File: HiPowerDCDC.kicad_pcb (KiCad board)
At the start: 2 copper layers, 125.8 x 100 mm, 66 parts, among them J1 Conn_01x01, J2 Conn_01x01, J3 Conn_01x01, J4 Conn_01x01, J5 Conn_01x04, Q1 WMJ38N60, Q2 WMJ38N60, SW1 SW_Push, SW2 SW_Push, U1 ESP32-WROOM-32U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

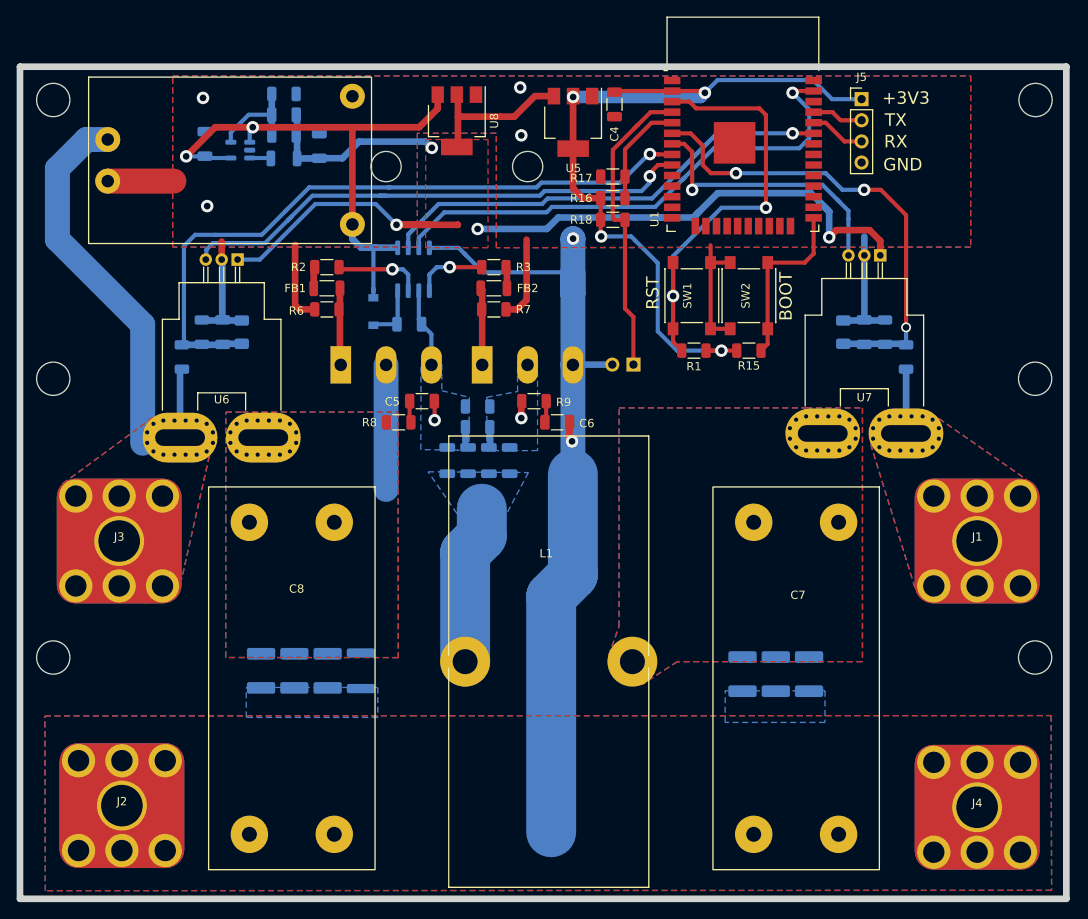
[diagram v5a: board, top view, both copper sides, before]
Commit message: Changed ACS770 to CC6900
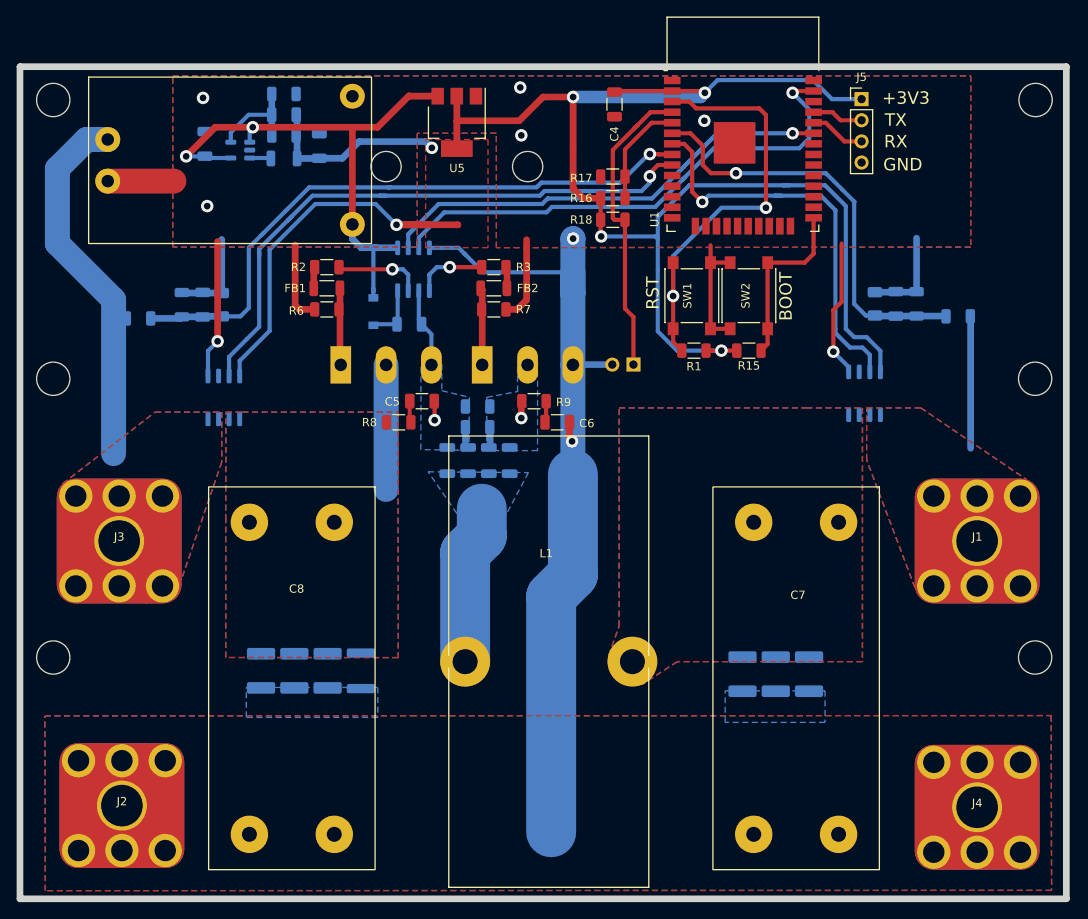
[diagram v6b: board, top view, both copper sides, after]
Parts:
- removed U8: AMS1117-5.0, Package_TO_SOT_SMD:SOT-223-3_TabPin2
- U6, U7: value ACS770xCB-050B-PFF -> CC6903SO-20A; footprint Sensor_Current:Allegro_CB_PFF -> Package_SO:SO-8_3.9x4.9mm_P1.27mm; moved to B.Cu
- moved U7 16.7 mm to (200.0, 92.2), turned to 90 degrees
- moved U6 16.7 mm to (123.0, 92.8), turned to 90 degrees
- moved U5 14.0 mm to (151.0, 59.7)
- moved R11 7.94 mm to (211.2, 83.0), turned to 180 degrees
- moved R13 6.97 mm to (112.8, 83.2), turned to 0 degrees
- moved C15 5.10 mm to (203.8, 81.5)
- moved D2 5.10 mm to (201.2, 81.5)
- moved R12 5.10 mm to (206.2, 81.5)
- moved C16 4.08 mm to (120.5, 81.6)
- moved D3 4.08 mm to (122.8, 81.6)
- moved R14 4.08 mm to (118.0, 81.6)
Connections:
- C17 pad 1: +5V -> +3V3
- C3 pad 1: +5V -> +3V3
- L2 pad 2: +5V -> +3V3
- R19 pad 1: +5V -> +3V3
- U5 pad 3: +5V -> +12V
- U6 pad 1: +5V -> VCC
- U6 pad 2: GND -> VCC
- U6 pad 3: CIN -> VDC
- U6 pad 5: VCC -> GND
- U7 pad 1: +5V -> Net-(J1-Pad1)
- U7 pad 2: GND -> Net-(J1-Pad1)
- U7 pad 3: COUT -> Net-(C11-Pad1)
- U7 pad 5: Net-(J1-Pad1) -> GND
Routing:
- net +3V3: track 95.6 -> 240.4 mm, vias 4 -> 6
- net +5V: track 135.9 -> 0.00 mm, vias 4 -> 0
- net GND: track 172.6 -> 199.7 mm, vias 6 -> 9
- net COUT: track 33.5 -> 49.1 mm
- net VDC: track 53.1 -> 44.5 mm
- net Net-(J1-Pad1): track 12.9 -> 20.9 mm
- net VIN: track 82.4 -> 75.4 mm
- net VOUT: track 56.7 -> 50.6 mm, vias 3 -> 1
- net CIN: track 68.6 -> 73.1 mm
- net +12V: track 67.4 -> 66.3 mm
- added copper zone on F.Cu, net +3V3
- removed copper zone on F.Cu, net +5V

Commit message: Added logos and 3V3 enable pin
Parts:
- added G***: LOGO, LOGO, F.Cu at (115.5, 85.8)
- added J6: Conn_01x02, Connector_PinHeader_2.54mm:PinHeader_1x02_P2.54mm_Vertical, F.Cu at (161.5, 58.8)
- R18: value 1M -> 10k
- moved C4 13.0 mm to (157.0, 58.0), turned to 90 degrees
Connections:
- C17 pad 1: +3V3 -> +5V
- C3 pad 1: +3V3 -> +5V
- C4 pad 1: +3V3 -> +3.3VP
- L2 pad 2: +3V3 -> +5V
- R19 pad 1: +3V3 -> +5V
- U5 pad 2: +3V3 -> +3.3VP
- U5 pad 3: +12V -> +5V
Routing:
- net +3V3: track 240.4 -> 204.5 mm, vias 6 -> 5
- net +5V: track 0.00 -> 25.3 mm, vias 0 -> 1
- net +3.3VP: track 0.00 -> 17.2 mm
- net +12V: track 66.3 -> 51.3 mm
- net GND: track 199.7 -> 191.0 mm, vias 9 -> 8
- added copper zone on F.Cu, net +3.3VP
- removed copper zone on F.Cu, net +3V3
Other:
- board text added: "3V3 PS"
- board text added: "OUT+"
- board text added: "OUT-"
- board text added: "PV+"
- board text added: "PV-"

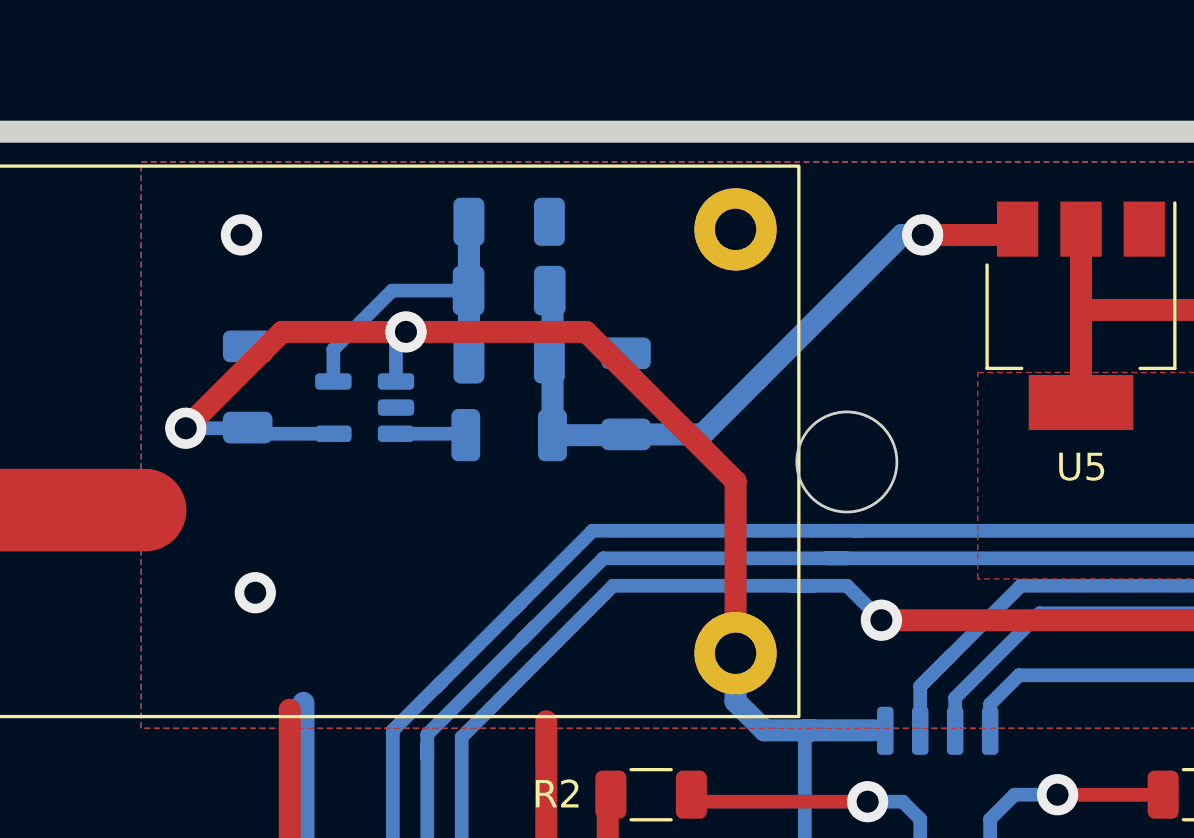
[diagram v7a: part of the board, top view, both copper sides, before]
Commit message: Added fan output and changed XT3410 to SD8942
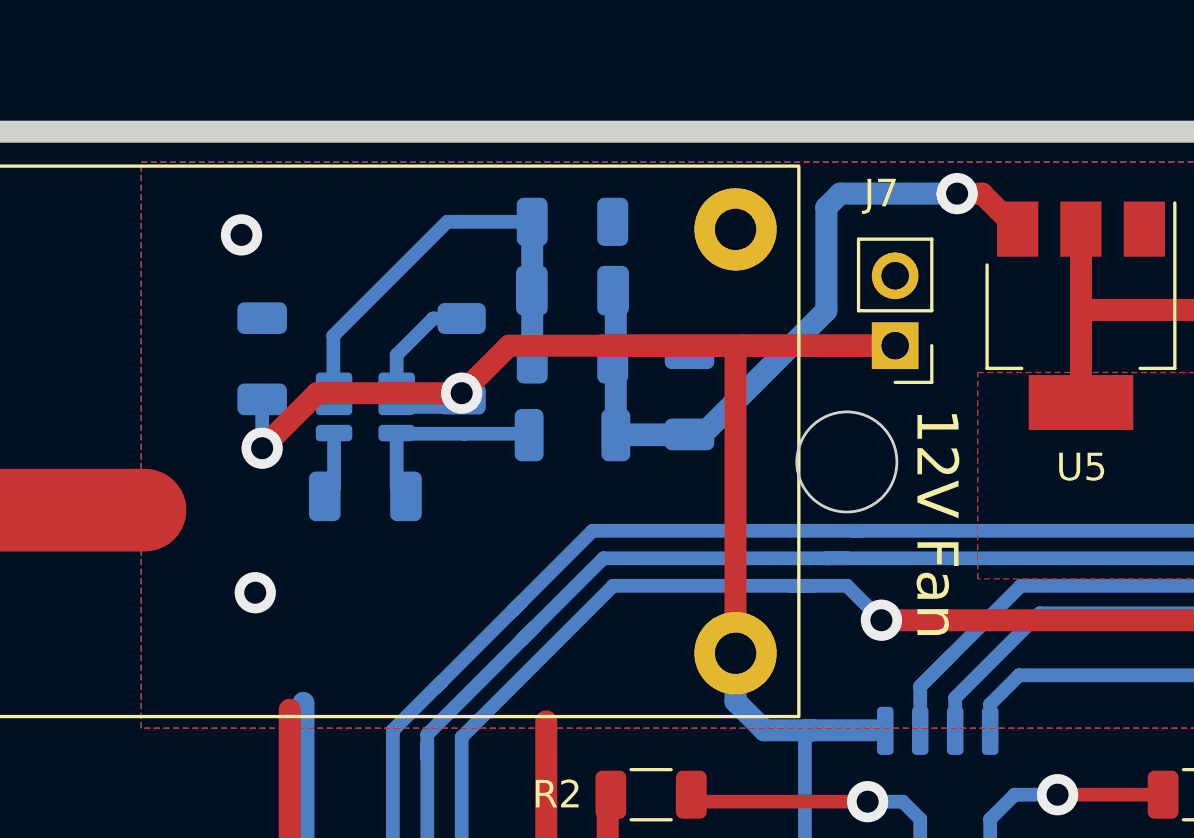
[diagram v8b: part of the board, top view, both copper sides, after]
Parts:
- added C18: 22n, Capacitor_SMD:C_1206_3216Metric, B.Cu at (125.0, 66.2)
- added J7: 12V vent., Connector_PinHeader_2.54mm:PinHeader_1x02_P2.54mm_Vertical, F.Cu at (144.2, 60.8)
- added R21: 100k, Resistor_SMD:R_1206_3216Metric, B.Cu at (128.5, 61.2)
- U4: value XT3410 -> SD8942; footprint Package_TO_SOT_SMD:SOT-23-5 -> Package_TO_SOT_SMD:SOT-23-6
- moved C17 2.30 mm to (132.5, 58.8)
- moved C3 2.30 mm to (136.8, 62.5)
- moved L2 2.30 mm to (132.5, 64.0)
- moved R19 2.30 mm to (132.5, 61.3)
- moved R20 2.30 mm to (132.5, 56.3)
- moved C1 1.15 mm to (121.2, 61.2)
- turned U4 to 0 degrees
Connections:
- U4 pad 1: +12V -> Net-(C18-Pad2)
- U4 pad 2: GND -> unconnected-(U4-Pad2)
- U4 pad 3: Net-(L2-Pad1) -> Net-(C17-Pad2)
- U4 pad 4: +12V -> Net-(U4-Pad4)
- U4 pad 5: Net-(C17-Pad2) -> +12V
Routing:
- net +12V: track 51.3 -> 64.7 mm
- net Net-(L2-Pad1): track 2.56 -> 7.30 mm
- net Net-(U4-Pad4): track 0.00 -> 3.85 mm
- net Net-(C17-Pad2): track 12.0 -> 15.6 mm
- net +5V: track 25.3 -> 28.9 mm
- net Net-(C18-Pad2): track 0.00 -> 2.44 mm
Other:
- board text added: "12V Fan"
